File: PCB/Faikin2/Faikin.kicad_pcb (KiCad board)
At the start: 2 copper layers, 70 x 70 mm, 28 parts, among them J1 1x5, J2 Prog, Q1 BSS138PS, U1 ESP32-PICO-MINI-02, U2 Barcode, U3 MD8942

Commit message: As ordered
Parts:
- added C3: 33pF, RevK:C_0402, F.Cu at (140.5, 60.0)
- added C4: 33pF, RevK:C_0402, F.Cu at (140.5, 57.5)
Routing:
- net G: track 12.6 -> 11.0 mm
- net Net-(Q1B-SP): track 8.30 -> 9.25 mm
- net Net-(Q1A-GN): track 4.44 -> 5.34 mm
- net DC: track 15.7 -> 15.1 mm
- net GND: vias 3 -> 6
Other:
- board text removed: "↑"
- board text removed: "↓"

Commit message: Tweak silk
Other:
- board text added: "Made in China"
- board text removed: "Made in China by JLCPCB"

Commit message: Silk screen
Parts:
- moved U2 1.40 mm to (153.5, 71.4)

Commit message: Silk
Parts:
- added Logo1: AJK, RevK:AJK, B.Cu at (135.0, 63.2)
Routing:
- net Net-(J2-0): track 30.9 -> 36.1 mm
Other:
- board text added: "Andrews & Arnold Ltd"
- board text added: "Made in China for"
- board text removed: "A"
- board text removed: "Made in China"

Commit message: Library update
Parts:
- removed R3: 10k, RevK:R_0402
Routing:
- net +3.3V: track 32.5 -> 28.5 mm

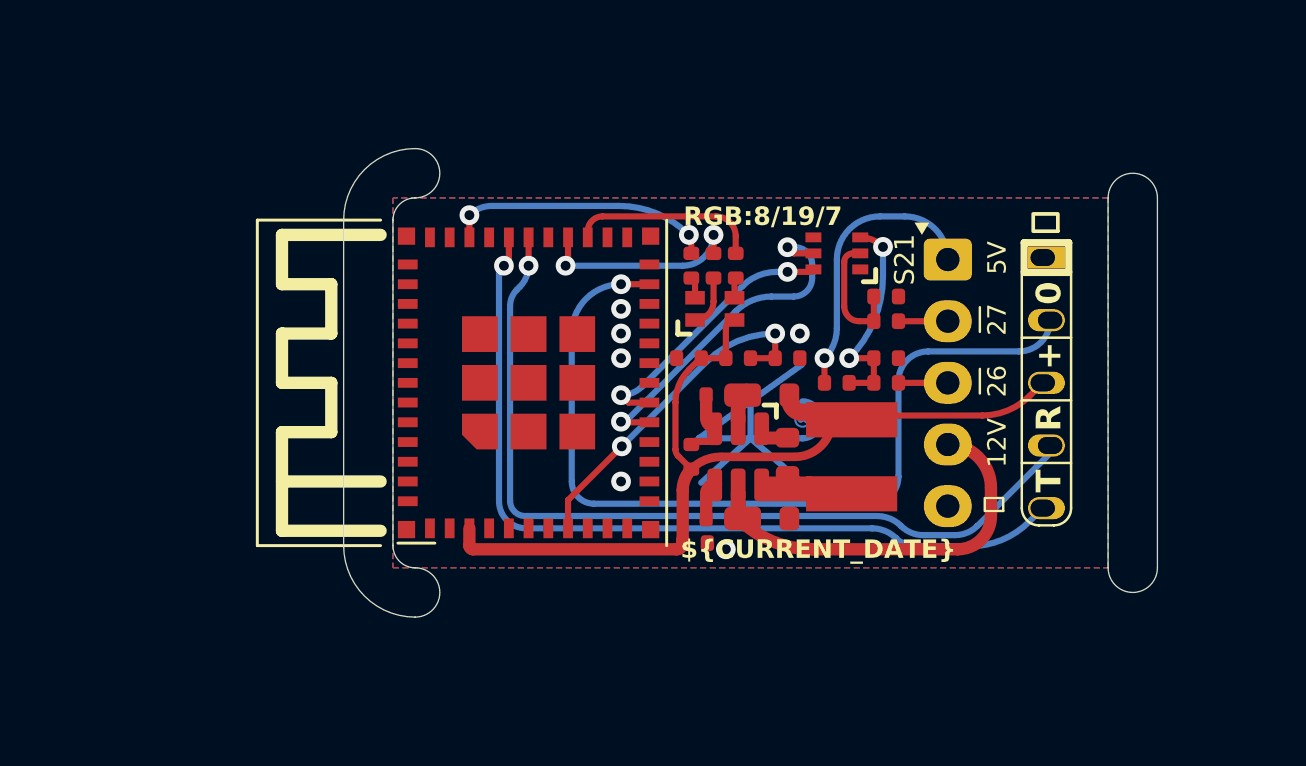
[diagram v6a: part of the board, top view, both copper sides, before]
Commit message: Faikin2 confirmed working, now replaces Faikin 1
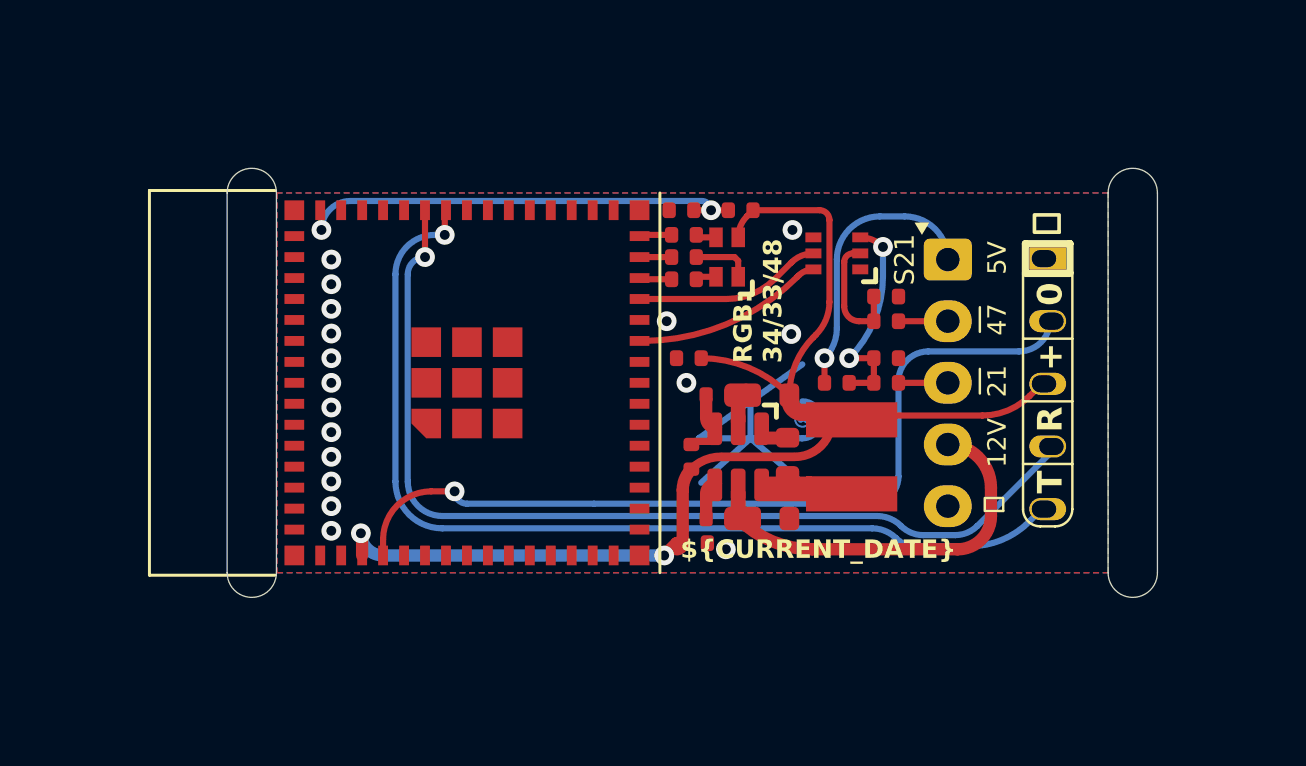
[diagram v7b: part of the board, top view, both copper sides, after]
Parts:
- removed C1: 1uF, RevK:C_0402
- removed J2: Prog, RevK:Shelly
- removed R4: 10K, RevK:R_0402
- removed U1: ESP32-PICO-MINI-02, RevK:ESP32-PICO-MINI-02
- added C6: 1uF, RevK:C_0402, F.Cu at (132.2, 54.0)
- added J3: Shelly, RevK:Shelly, F.Cu at (147.1, 61.0)
- added R3: 10K, RevK:R_0402, F.Cu at (134.6, 54.0)
- added U4: ESP32-S3-MINI-1, RevK:ESP32-S3-MINI-1, F.Cu at (123.5, 61.0)
- C5: value 100nF -> 22uF
- moved R12 2.44 mm to (132.3, 55.0), turned to 180 degrees
- moved D2 2.16 mm to (134.1, 55.9), turned to 90 degrees
- moved R5 1.25 mm to (132.3, 55.9), turned to 180 degrees
- moved R6 0.63 mm to (132.3, 56.8), turned to 180 degrees
- moved V1 0.20 mm to (135.0, 53.3)
- moved V2 0.20 mm to (135.0, 68.7)
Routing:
- net Net-(J3-Tx): track 0.00 -> 40.2 mm, vias 0 -> 1
- net Net-(J3-Rx): track 0.00 -> 39.7 mm, vias 0 -> 1
- net Net-(J2-0): track 35.9 -> 0.00 mm, vias 1 -> 0
- net Net-(J3-0): track 0.00 -> 34.8 mm, vias 0 -> 1
- net Net-(J2-Rx): track 34.6 -> 0.00 mm, vias 1 -> 0
- net Net-(J2-Tx): track 34.2 -> 0.00 mm, vias 1 -> 0
- net Net-(U4-EN): track 0.00 -> 18.8 mm, vias 0 -> 2
- net EN: track 14.2 -> 0.00 mm, vias 2 -> 0
- net +3.3V: track 28.5 -> 42.2 mm, vias 0 -> 2
- net G: track 11.0 -> 1.32 mm, vias 2 -> 0
- net R: track 8.62 -> 1.30 mm, vias 2 -> 0
- net TX: track 14.4 -> 7.62 mm, vias 2 -> 0
- net B: track 7.44 -> 1.32 mm
- net RX: track 11.0 -> 7.78 mm, vias 2 -> 0
- net GND: vias 6 -> 17
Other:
- board text added: "21"
- board text added: "47"
- board text added: "RGB: 34/33/48"
- board text removed: "RGB:8/19/7"

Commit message: Smaller
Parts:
- moved C5 5.50 mm to (138.0, 60.0)
- moved C6 2.70 mm to (134.9, 54.0)
- moved R3 2.70 mm to (137.3, 54.0)
- moved D2 2.60 mm to (136.7, 55.9)
- moved R12 2.60 mm to (134.9, 55.0)
- moved R5 2.60 mm to (134.9, 55.9)
- moved R6 2.60 mm to (134.9, 56.8)
- moved U4 2.60 mm to (126.1, 61.0)
- moved C2 2.25 mm to (135.0, 67.5)
- moved C10 2.00 mm to (138.5, 64.0)
- moved C8 2.00 mm to (137.8, 66.5)
- moved C9 2.00 mm to (137.8, 61.5)
- moved L2 2.00 mm to (141.1, 64.0)
- moved R10 2.00 mm to (135.7, 61.5)
- moved R11 2.00 mm to (135.7, 66.5)
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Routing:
- net +3.3V: track 42.2 -> 65.9 mm
- net Net-(J3-0): track 34.8 -> 41.0 mm
- net DC: track 15.1 -> 9.45 mm, vias 0 -> 1
- net Net-(J3-Tx): track 40.2 -> 36.3 mm
- net Net-(J3-Rx): track 39.7 -> 41.9 mm
- net GND: track 0.00 -> 1.20 mm, vias 17 -> 11
- net Net-(Q1B-SP): track 8.88 -> 9.57 mm
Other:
- board text added: "34/33/48"
- board text removed: "RGB: 34/33/48"
